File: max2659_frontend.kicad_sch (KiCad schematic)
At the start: 4 parts, among them U1 MAX2659 (see BOM note)

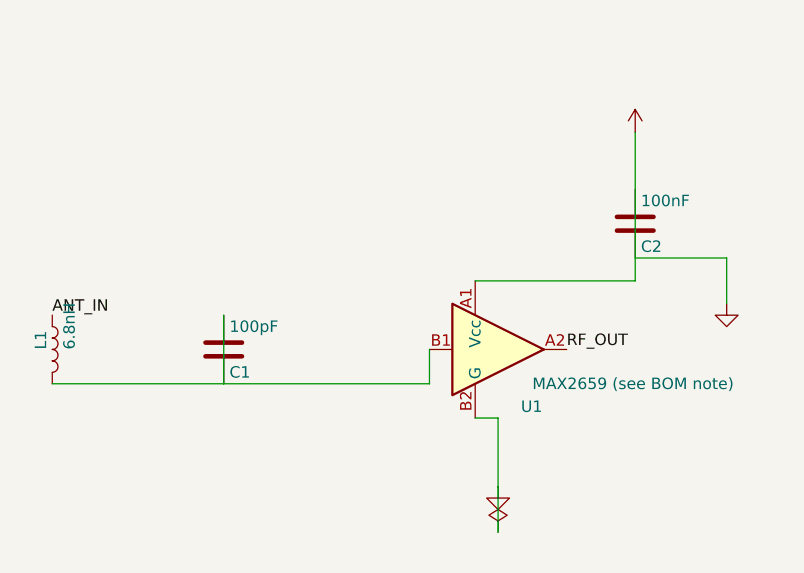
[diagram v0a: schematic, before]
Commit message: MILESTONE: clean, correctly laid out, ERC-validated MAX2659 schematic - rotated L1/C1 to align pin heights, eliminating wire overlap and ambiguous crossings from earlier attempts
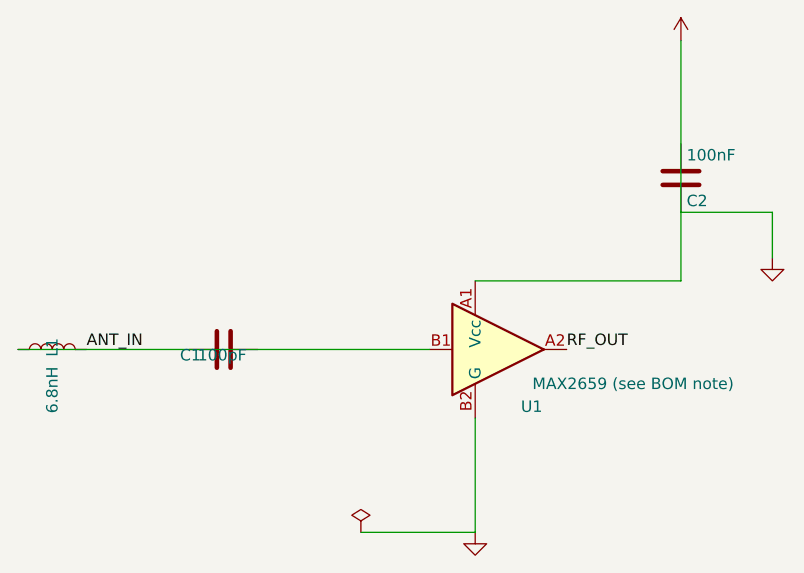
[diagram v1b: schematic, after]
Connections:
- net ANT_IN: now also L1.2, U1.B1
- now unconnected: C1.1, C1.2
